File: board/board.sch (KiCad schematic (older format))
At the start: 11 parts, among them J1 RJ45, P8 BeagleBone_Black_Header, P9 BeagleBone_Black_Header, U1 7438

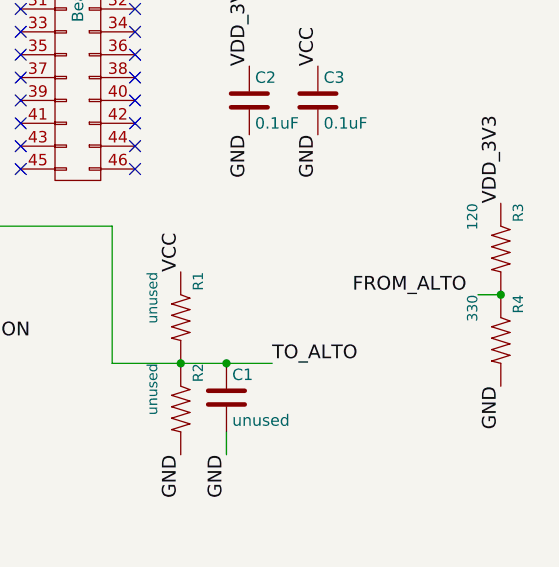
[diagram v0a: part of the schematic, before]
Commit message: Rename boardv2 to board. Replace the Eagle version with the KiCad version
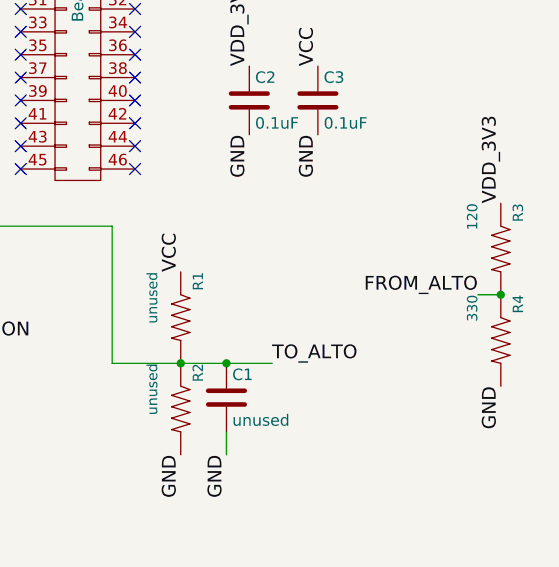
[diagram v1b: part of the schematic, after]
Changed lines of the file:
@@
 Wire Wire Line
 	7000 3900 6900 3900
-Text Label 6850 3900 2    60   ~ 0
+Text Label 6900 3900 2    60   ~ 0
 FROM_ALTO
 Text Label 7000 4300 3    60   ~ 0
